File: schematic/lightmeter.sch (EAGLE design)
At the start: 76 parts, among them J1 CONNECTEDJUMPER, J2 CONNECTEDJUMPER, J3 CONNECTEDJUMPER, J4 CONNECTEDJUMPER, J5 CONNECTEDJUMPER, J6 CONNECTEDJUMPER, Q1 PCHANNELMOSFETSOT-523-3

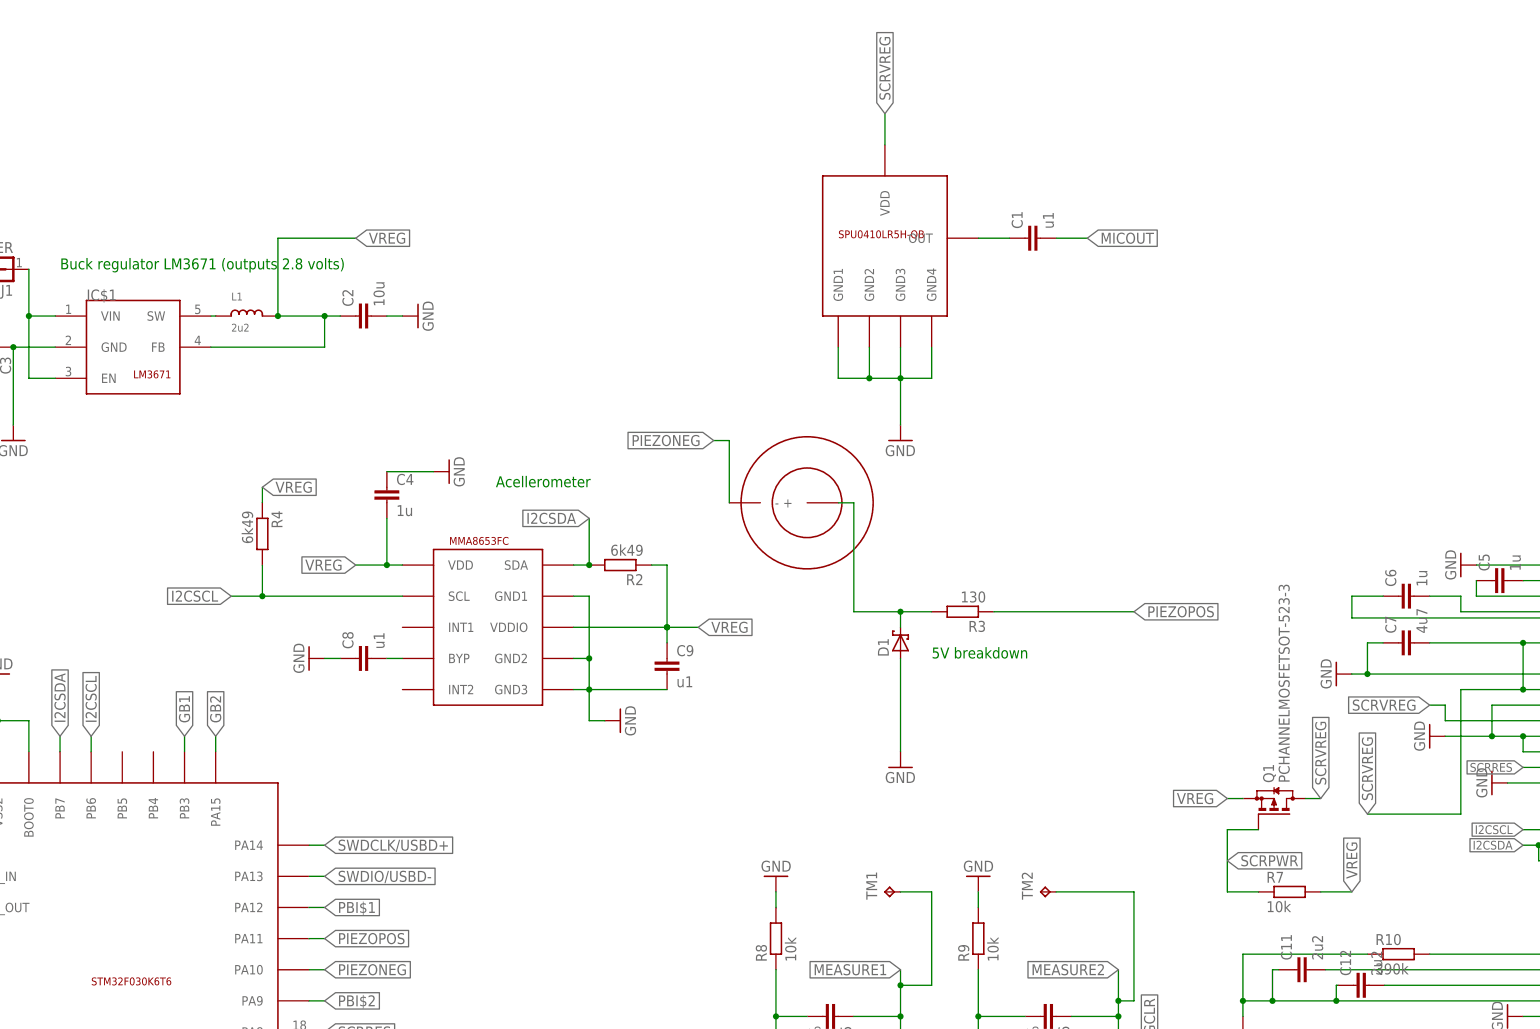
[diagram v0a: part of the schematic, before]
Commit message: Experiment with getting rid of screen/mic power mosfet
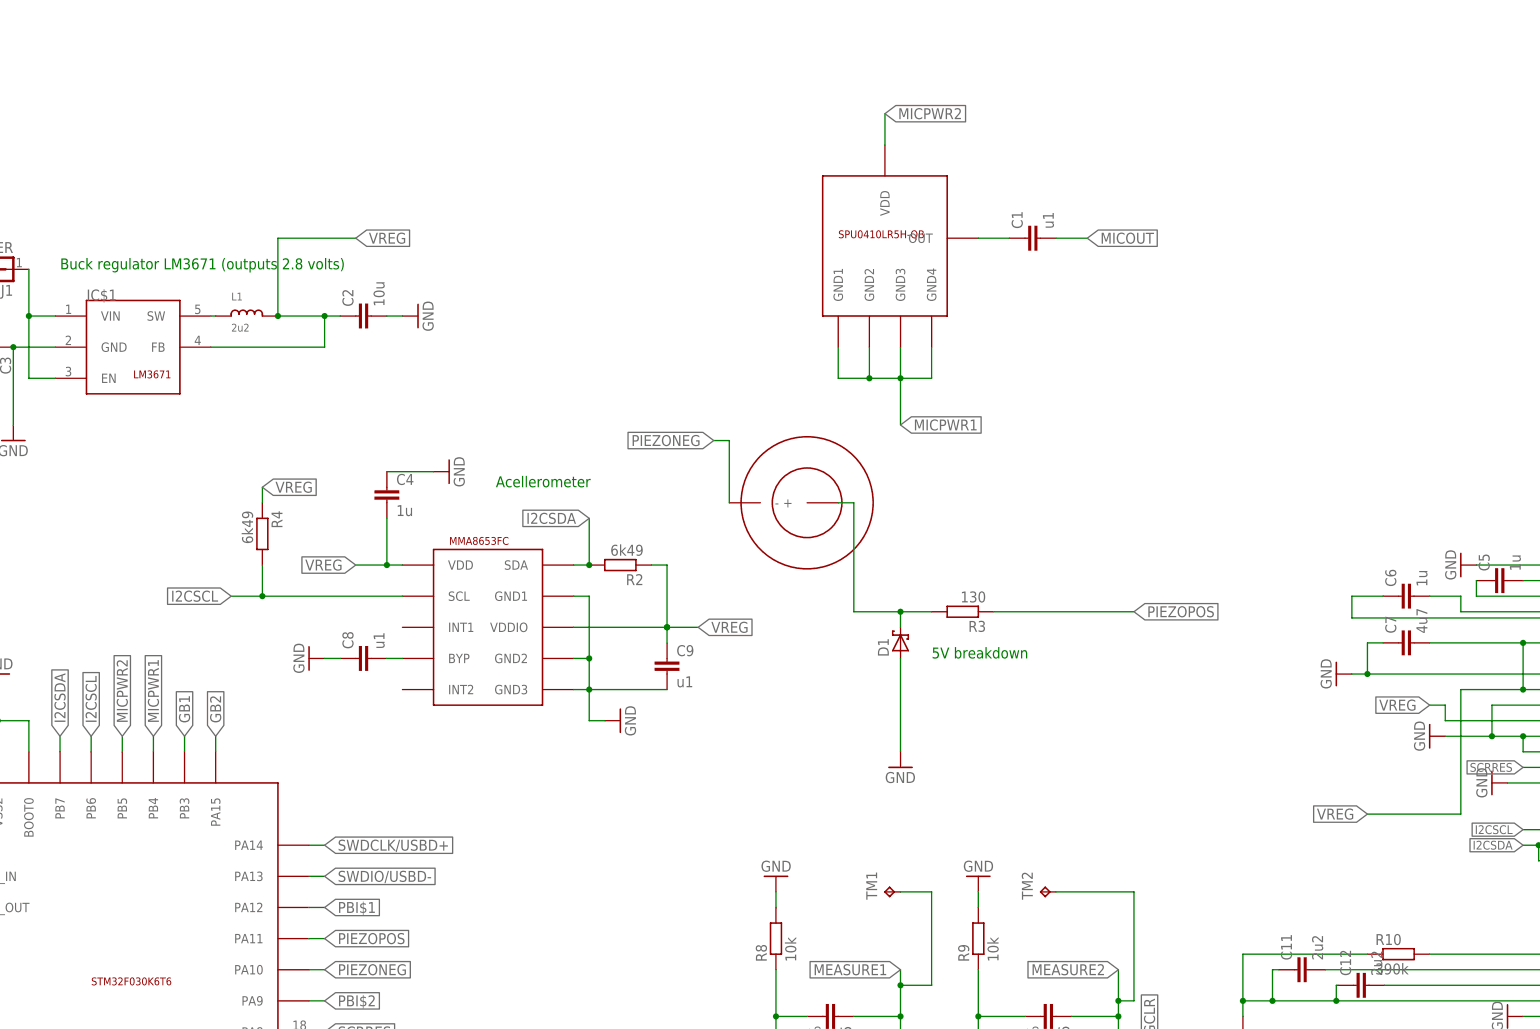
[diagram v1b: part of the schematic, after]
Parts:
- removed Q1: PCHANNELMOSFETSOT-523-3, lightmeter:PCHANNELMOSFETSOT-523-3
- removed R7: 10k, resistor:R-EU_R0402
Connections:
- removed net SCRVREG: C7.2, IC$3.BS1, IC$3.VBAT, IC$3.VDD, Q1.D, U$1.VDD
- new net MICPWR1: IC$4.PB4, U$1.GND1, U$1.GND2, U$1.GND3, U$1.GND4
- new net MICPWR2: IC$4.PB5, U$1.VDD
- net GND: no longer U$1.GND1, U$1.GND2, U$1.GND3, U$1.GND4
- net SCRPWR: no longer Q1.G, R7.1
- net VREG: now also C7.2, IC$3.BS1, IC$3.VBAT, IC$3.VDD; no longer Q1.S, R7.2

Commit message: Revert "Experiment with getting rid of screen/mic power mosfet"
This reverts commit 0ea2fc8952a41135a350a53187906d9f9b76826a.
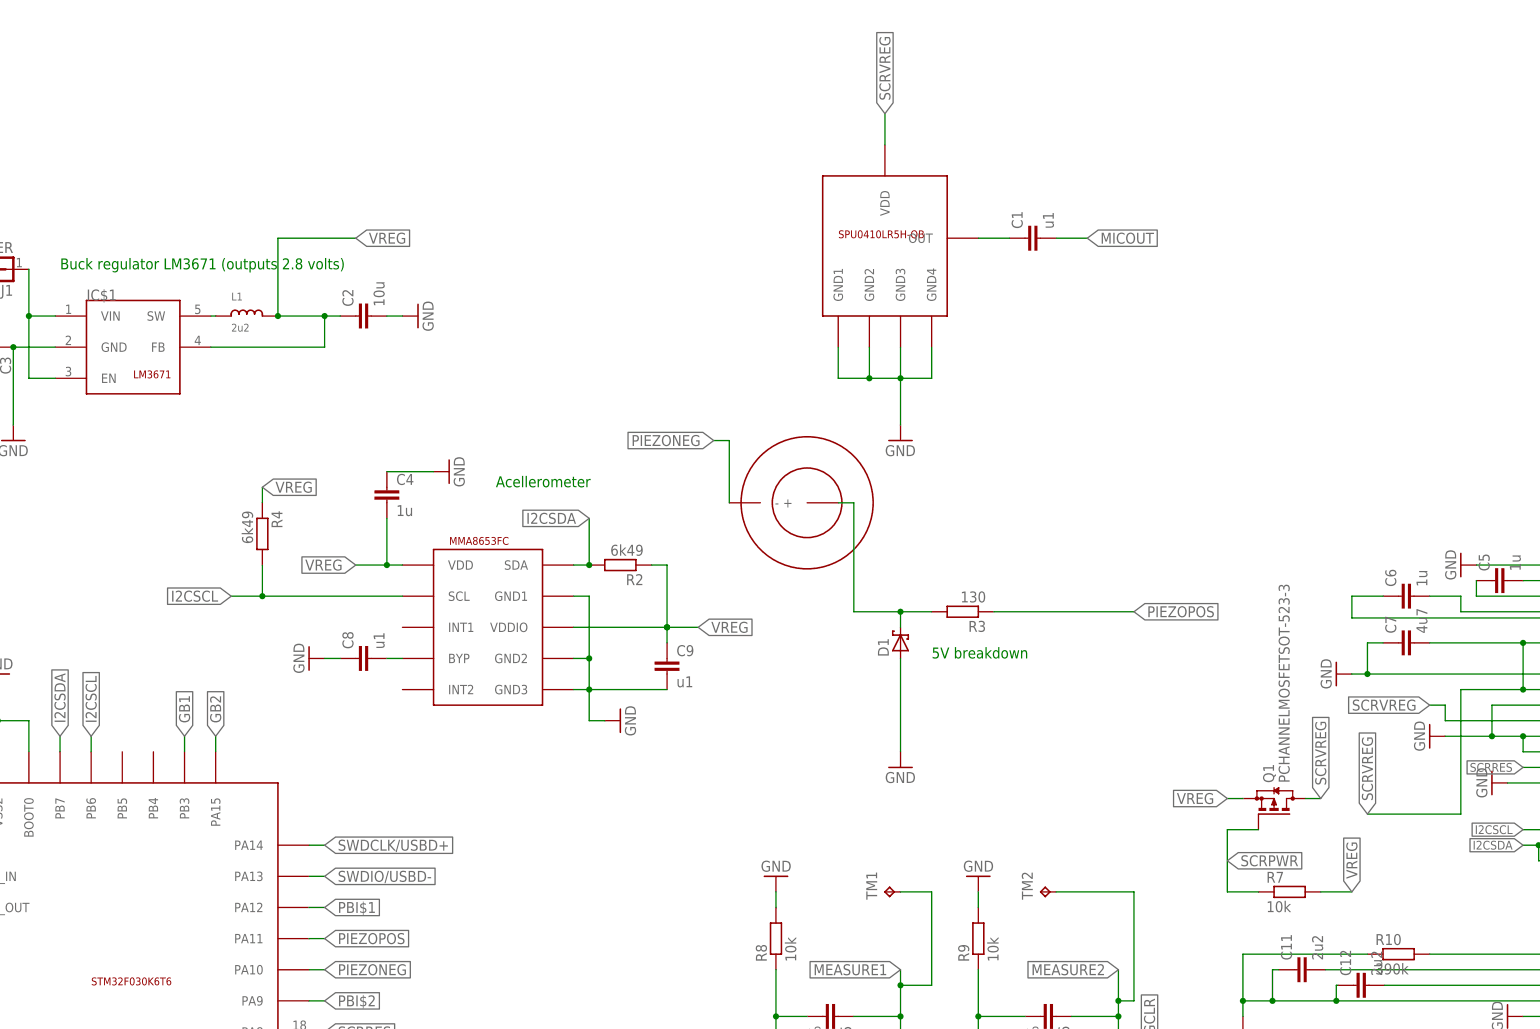
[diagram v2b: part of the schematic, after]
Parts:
- added Q1: PCHANNELMOSFETSOT-523-3, lightmeter:PCHANNELMOSFETSOT-523-3
- added R7: 10k, resistor:R-EU_R0402
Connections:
- removed net MICPWR1: IC$4.PB4, U$1.GND1, U$1.GND2, U$1.GND3, U$1.GND4
- removed net MICPWR2: IC$4.PB5, U$1.VDD
- new net SCRVREG: C7.2, IC$3.BS1, IC$3.VBAT, IC$3.VDD, Q1.D, U$1.VDD
- net GND: now also U$1.GND1, U$1.GND2, U$1.GND3, U$1.GND4
- net SCRPWR: now also Q1.G, R7.1
- net VREG: now also Q1.S, R7.2; no longer C7.2, IC$3.BS1, IC$3.VBAT, IC$3.VDD

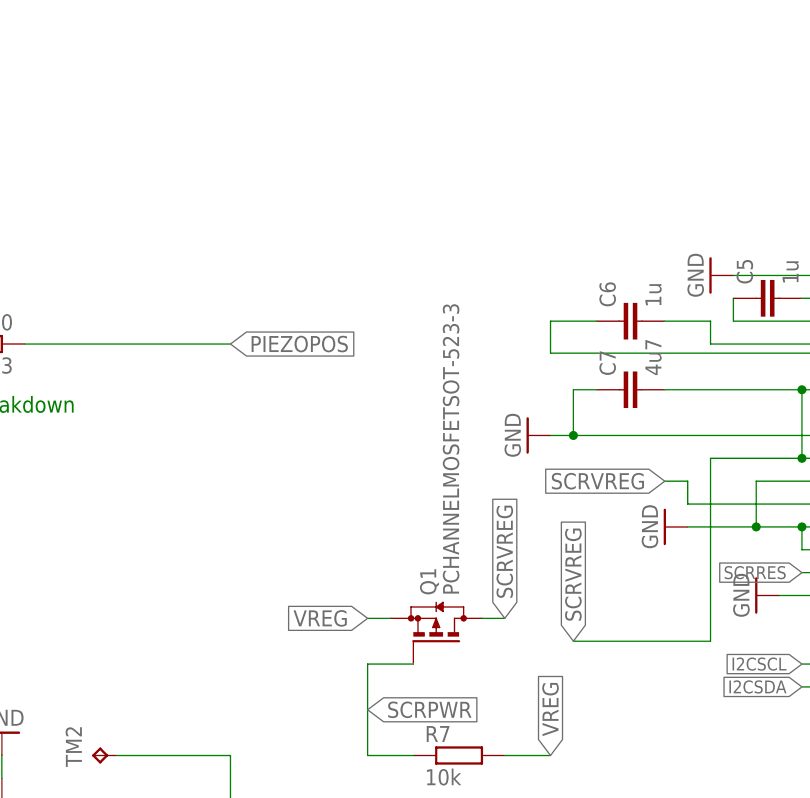
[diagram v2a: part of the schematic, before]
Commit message: Fix issue with pins being wrong way round for screen power MOSFET.
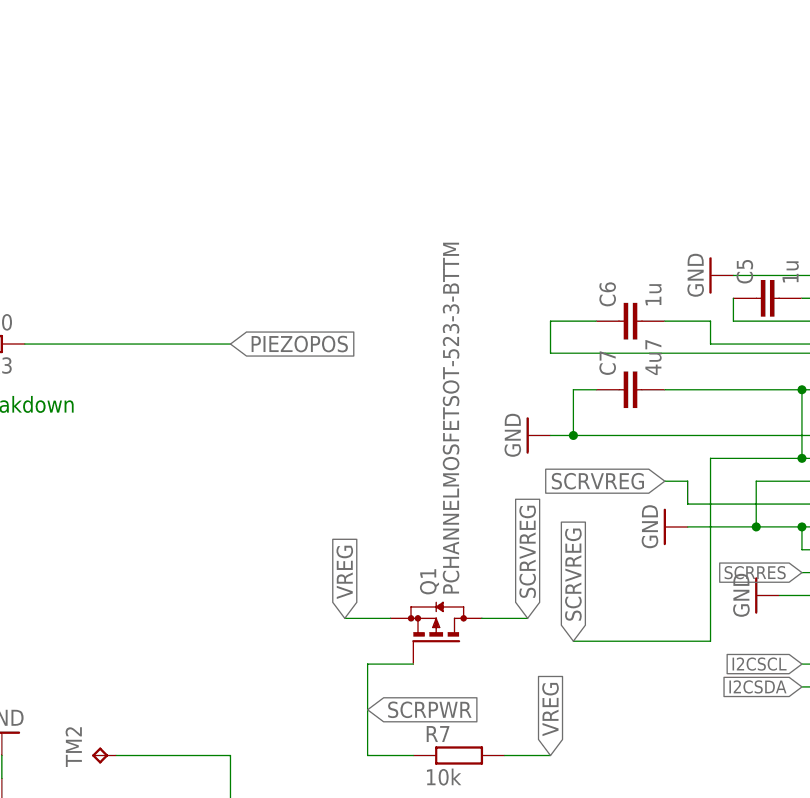
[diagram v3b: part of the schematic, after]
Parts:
- Q1: value PCHANNELMOSFETSOT-523-3 -> PCHANNELMOSFETSOT-523-3-BTTM; device lightmeter:PCHANNELMOSFETSOT-523-3 -> lightmeter:PCHANNELMOSFETSOT-523-3-BTTM

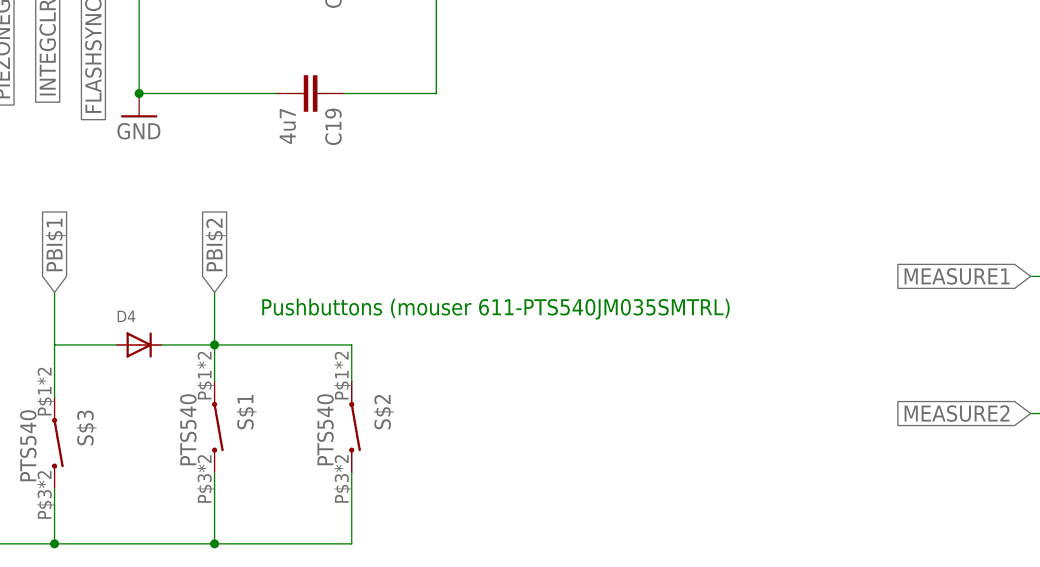
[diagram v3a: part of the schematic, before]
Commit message: Fix button logic by adding additional diode.
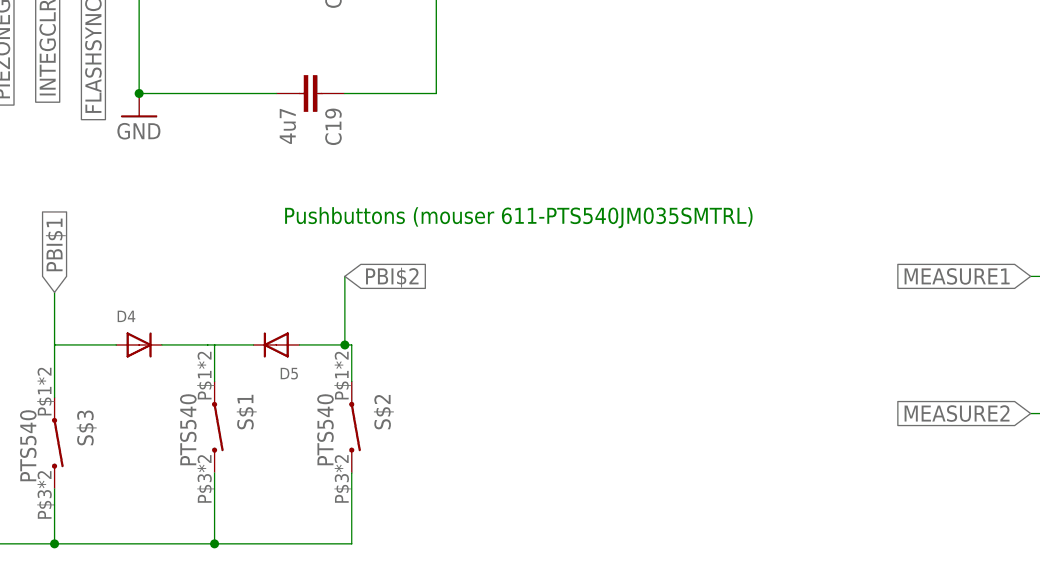
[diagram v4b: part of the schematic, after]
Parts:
- added D5: (no value), adafruit:DIODESOD-323F
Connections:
- new net N$13: D4.C, D5.C, S$1.1
- net PBI$2: now also D5.A; no longer D4.C, S$1.1
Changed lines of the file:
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@@
 <part name="R6" library="resistor" deviceset="R-EU_" device="R0402" value="??"/>
 <part name="Q1" library="lightmeter" deviceset="PCHANNELMOSFET" device="SOT-523-3-BTTM" value="PCHANNELMOSFETSOT-523-3-BTTM"/>
+<part name="D5" library="adafruit" deviceset="DIODE" device="SOD-323F"/>
 </parts>
 <sheets>
@@
 <text x="-152.4" y="-7.62" size="1.778" layer="91">Battery (3.7V nominal)</text>
 <text x="-40.64" y="101.6" size="1.778" layer="91">Buck regulator LM3671 (outputs 2.8 volts)</text>
-<text x="-1.778" y="-83.058" size="1.778" layer="91">Pushbuttons (mouser 611-PTS540JM035SMTRL)</text>
+<text x="0.762" y="-72.898" size="1.778" layer="91">Pushbuttons (mouser 611-PTS540JM035SMTRL)</text>
 <text x="213.36" y="60.96" size="1.778" layer="91">Screen (C2P right, IREF left)</text>
 <text x="-152.4" y="-27.94" size="1.778" layer="91">Power muxer</text>
@@
 <instance part="R6" gate="G$1" x="-83.82" y="2.54" rot="R180"/>
 <instance part="Q1" gate="G$1" x="157.48" y="15.24" rot="R90"/>
+<instance part="D5" gate="G$1" x="0" y="-86.36" rot="R180"/>
 </instances>
 <busses>
@@
 <wire x1="8.382" y1="-90.424" x2="8.382" y2="-86.36" width="0.1524" layer="91"/>
 <pinref part="S$2" gate="G$1" pin="1"/>
-<pinref part="S$1" gate="G$1" pin="1"/>
-<wire x1="-6.858" y1="-80.518" x2="-6.858" y2="-86.36" width="0.1524" layer="91"/>
-<label x="-6.858" y="-80.518" size="1.778" layer="95" rot="R90" xref="yes"/>
-<wire x1="-6.858" y1="-86.36" x2="-6.858" y2="-90.424" width="0.1524" layer="91"/>
-<wire x1="-12.7" y1="-86.36" x2="-6.858" y2="-86.36" width="0.1524" layer="91"/>
-<junction x="-6.858" y="-86.36"/>
-<wire x1="-6.858" y1="-86.36" x2="8.382" y2="-86.36" width="0.1524" layer="91"/>
-<pinref part="D4" gate="G$1" pin="C"/>
+<wire x1="7.62" y1="-86.36" x2="8.382" y2="-86.36" width="0.1524" layer="91"/>
+<wire x1="7.62" y1="-86.36" x2="7.62" y2="-78.74" width="0.1524" layer="91"/>
+<label x="7.62" y="-78.74" size="1.778" layer="95" xref="yes"/>
+<pinref part="D5" gate="G$1" pin="A"/>
+<wire x1="2.54" y1="-86.36" x2="7.62" y2="-86.36" width="0.1524" layer="91"/>
+<junction x="7.62" y="-86.36"/>
 </segment>
 <segment>
@@
 </segment>
 </net>
+<net name="N$13" class="0">
+<segment>
+<pinref part="S$1" gate="G$1" pin="1"/>
+<wire x1="-6.858" y1="-86.36" x2="-6.858" y2="-90.424" width="0.1524" layer="91"/>
+<pinref part="D4" gate="G$1" pin="C"/>
+<wire x1="-12.7" y1="-86.36" x2="-7.62" y2="-86.36" width="0.1524" layer="91"/>
+<pinref part="D5" gate="G$1" pin="C"/>
+<wire x1="-7.62" y1="-86.36" x2="-6.858" y2="-86.36" width="0.1524" layer="91"/>
+<wire x1="-6.858" y1="-86.36" x2="-2.54" y2="-86.36" width="0.1524" layer="91"/>
+</segment>
+</net>

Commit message: Some work on board/schematic.
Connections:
- new net LREGENABLE: IC$6.EN
- net VCC: no longer IC$6.EN
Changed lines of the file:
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@@
 <wire x1="-106.68" y1="-66.04" x2="-106.68" y2="-71.12" width="0.1524" layer="91"/>
 <junction x="-106.68" y="-71.12"/>
-<pinref part="IC$6" gate="G$1" pin="EN"/>
-<wire x1="-104.14" y1="-86.36" x2="-106.68" y2="-86.36" width="0.1524" layer="91"/>
-<wire x1="-106.68" y1="-86.36" x2="-106.68" y2="-71.12" width="0.1524" layer="91"/>
 </segment>
 <segment>
@@
 </segment>
 </net>
+<net name="LREGENABLE" class="0">
+<segment>
+<pinref part="IC$6" gate="G$1" pin="EN"/>
+<wire x1="-104.14" y1="-86.36" x2="-106.68" y2="-86.36" width="0.1524" layer="91"/>
+<label x="-106.68" y="-86.36" size="1.778" layer="95" rot="R180" xref="yes"/>
+</segment>
+</net>

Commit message: Some work on board and schematic.
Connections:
- net LREGENABLE: now also IC$4.PB5
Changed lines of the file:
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@@
 <label x="-106.68" y="-86.36" size="1.778" layer="95" rot="R180" xref="yes"/>
+</segment>
+<segment>
+<pinref part="IC$4" gate="G$1" pin="PB5"/>
+<wire x1="-30.48" y1="22.86" x2="-30.48" y2="25.4" width="0.1524" layer="91"/>
+<label x="-30.48" y="25.4" size="1.778" layer="95" rot="R90" xref="yes"/>
 </segment>
 </net>
